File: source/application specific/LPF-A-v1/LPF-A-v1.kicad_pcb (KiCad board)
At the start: 6 copper layers, 32 x 20 mm, 33 parts, among them J1 Conn_01x01_Pin, J2 Conn_01x01_Pin, J3 Conn_01x01_Pin, J4 Conn_01x01_Pin, J5 Conn_01x01_Pin, J6 Conn_01x01_Pin, J7 Conn_01x01_Pin, U1 OPA140, U2 OPA140

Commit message: Added pad for external resistor input
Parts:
- added J8: Conn_01x01_Pin, Manhattan:Manhattan-2mm, F.Cu at (164.5, 101.5)
- R1: footprint Resistor_SMD:R_1206_3216Metric_Pad1.30x1.75mm_HandSolder -> Resistor_SMD:R_0805_2012Metric_Pad1.20x1.40mm_HandSolder
- moved R1 0.75 mm to (140.0, 101.5)
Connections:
- net Debug renamed InR
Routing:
- net InR: track 23.1 -> 26.7 mm
- net In: track 2.20 -> 3.50 mm
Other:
- board text added: "IN R"
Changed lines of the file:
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@@
 	(net 11 "In")
 	(net 12 "Bias")
-	(net 13 "Debug")
+	(net 13 "InR")
 	(net 14 "Net-(U2--)")
 	(net 15 "U2 V+")
@@
 	(net 23 "Net-(U1-+)")
 	(net 24 "Net-(U2-+)")
+	(footprint "Manhattan:Manhattan-2mm"
+		(layer "F.Cu")
+		(at 164.5 101.5)
+		(property "Reference" "J8"
+			(at 0 -1.905 0)
+			(unlocked yes)
+			(layer "F.SilkS")
+			(hide yes)
+			(effects
+				(font
+					(size 1 1)
+					(thickness 0.1)
+				)
+			)
+		)
+		(property "Value" "Conn_01x01_Pin"
+			(at 0 1.675 0)
+			(unlocked yes)
+			(layer "F.Fab")
+			(hide yes)
+			(effects
+				(font
+					(size 1 1)
+					(thickness 0.15)
+				)
+			)
+		)
+		(property "Footprint" "Manhattan:Manhattan-2mm"
+			(at 0 0 0)
+			(unlocked yes)
+			(layer "F.Fab")
+			(hide yes)
+			(effects
+				(font
+					(size 1 1)
+					(thickness 0.15)
+				)
+			)
+		)
+		(property "Datasheet" ""
+			(at 0 0 0)
+			(unlocked yes)
+			(layer "F.Fab")
+			(hide yes)
+			(effects
+				(font
+					(size 1 1)
+					(thickness 0.15)
+				)
+			)
+		)
+		(property "Description" "Generic connector, single row, 01x01, script generated"
+			(at 0 0 0)
+			(unlocked yes)
+			(layer "F.Fab")
+			(hide yes)
+			(effects
+				(font
+					(size 1 1)
+					(thickness 0.15)
+				)
+			)
+		)
+		(property ki_fp_filters "Connector*:*_1x??_*")
+		(sheetname "Root")
+		(sheetfile "LPF-A-v1.kicad_sch")
+		(attr smd)
+		(fp_text user "${REFERENCE}"
+			(at 0 3.175 0)
+			(unlocked yes)
+			(layer "F.Fab")
+			(effects
+				(font
+					(size 1 1)
+					(thickness 0.15)
+				)
+			)
+		)
+		(pad "1" smd roundrect
+			(at 0 0)
+			(size 2 2)
+			(layers "F.Cu" "F.Paste" "F.Mask")
+			(roundrect_rratio 0.125)
+			(net 13 "InR")
+			(pinfunction "Pin_1")
+			(pintype "passive")
+			(thermal_bridge_angle 45)
+		)
+	)
 	(footprint "Resistor_SMD:R_0603_1608Metric_Pad0.98x0.95mm_HandSolder"
 		(layer "F.Cu")
@@
 			(layers "F.Cu" "F.Paste" "F.Mask")
 			(roundrect_rratio 0.15873)
-			(net 13 "Debug")
+			(net 13 "InR")
 			(pintype "passive")
 		)
@@
 			(layers "F.Cu" "F.Paste" "F.Mask")
 			(roundrect_rratio 0.15873)
-			(net 13 "Debug")
+			(net 13 "InR")
 			(pintype "passive")
 		)
@@
 			(layers "F.Cu" "F.Paste" "F.Mask")
 			(roundrect_rratio 0.25)
-			(net 13 "Debug")
+			(net 13 "InR")
 			(pintype "passive")
 		)
@@
 			(layers "F.Cu" "F.Paste" "F.Mask")
 			(roundrect_rratio 0.15873)
-			(net 13 "Debug")
+			(net 13 "InR")
 			(pintype "passive")
 		)
@@
 		)
 	)
-	(footprint "Resistor_SMD:R_1206_3216Metric_Pad1.30x1.75mm_HandSolder"
+	(footprint "Resistor_SMD:R_0805_2012Metric_Pad1.20x1.40mm_HandSolder"
 		(layer "F.Cu")
-		(at 139.25 101.5)
-		(descr "Resistor SMD 1206 (3216 Metric), square (rectangular) end terminal, IPC_7351 nominal with elongated pad for handsoldering. (Body size source: IPC-SM-782 page 72, https://www.pcb-3d.com/wordpress/wp-content/uploads/ipc-sm-782a_amendment_1_and_2.pdf), generated with kicad-footprint-generator")
+		(at 140 101.5)
+		(descr "Resistor SMD 0805 (2012 Metric), square (rectangular) end terminal, IPC_7351 nominal with elongated pad for handsoldering. (Body size source: IPC-SM-782 page 72, https://www.pcb-3d.com/wordpress/wp-content/uploads/ipc-sm-782a_amendment_1_and_2.pdf), generated with kicad-footprint-generator")
 		(tags "resistor handsolder")
 		(property "Reference" "R1"
-			(at 0 -1.82 0)
+			(at 0 -1.65 0)
 			(layer "F.SilkS")
 			(hide yes)
@@
 		)
 		(property "Value" "47k"
-			(at 0 1.82 0)
+			(at 0 1.65 0)
 			(layer "F.Fab")
 			(hide yes)
@@
 			)
 		)
-		(property "Footprint" "Resistor_SMD:R_1206_3216Metric_Pad1.30x1.75mm_HandSolder"
+		(property "Footprint" "Resistor_SMD:R_0805_2012Metric_Pad1.20x1.40mm_HandSolder"
 			(at 0 0 0)
 			(layer "F.Fab")
@@
 		(attr smd)
 		(fp_line
-			(start -0.727064 -0.91)
-			(end 0.727064 -0.91)
+			(start -0.227064 -0.735)
+			(end 0.227064 -0.735)
 			(stroke
 				(width 0.12)
@@
 		)
 		(fp_line
-			(start -0.727064 0.91)
-			(end 0.727064 0.91)
+			(start -0.227064 0.735)
+			(end 0.227064 0.735)
 			(stroke
 				(width 0.12)
@@
 		)
 		(fp_line
-			(start -2.45 -1.12)
-			(end 2.45 -1.12)
+			(start -1.85 -0.95)
+			(end 1.85 -0.95)
 			(stroke
 				(width 0.05)
@@
 		)
 		(fp_line
-			(start -2.45 1.12)
-			(end -2.45 -1.12)
+			(start -1.85 0.95)
+			(end -1.85 -0.95)
 			(stroke
 				(width 0.05)
@@
 		)
 		(fp_line
-			(start 2.45 -1.12)
-			(end 2.45 1.12)
+			(start 1.85 -0.95)
+			(end 1.85 0.95)
 			(stroke
 				(width 0.05)
@@
 		)
 		(fp_line
-			(start 2.45 1.12)
-			(end -2.45 1.12)
+			(start 1.85 0.95)
+			(end -1.85 0.95)
 			(stroke
 				(width 0.05)
@@
 		)
 		(fp_line
-			(start -1.6 -0.8)
-			(end 1.6 -0.8)
+			(start -1 -0.625)
+			(end 1 -0.625)
 			(stroke
 				(width 0.1)
@@
 		)
 		(fp_line
-			(start -1.6 0.8)
-			(end -1.6 -0.8)
+			(start -1 0.625)
+			(end -1 -0.625)
 			(stroke
 				(width 0.1)
@@
 		)
 		(fp_line
-			(start 1.6 -0.8)
-			(end 1.6 0.8)
+			(start 1 -0.625)
+			(end 1 0.625)
 			(stroke
 				(width 0.1)
@@
 		)
 		(fp_line
-			(start 1.6 0.8)
-			(end -1.6 0.8)
+			(start 1 0.625)
+			(end -1 0.625)
 			(stroke
 				(width 0.1)
@@
 			(effects
 				(font
-					(size 0.8 0.8)
-					(thickness 0.12)
+					(size 0.5 0.5)
+					(thickness 0.08)
 				)
 			)
 		)
 		(pad "1" smd roundrect
-			(at -1.55 0)
-			(size 1.3 1.75)
+			(at -1 0)
+			(size 1.2 1.4)
 			(layers "F.Cu" "F.Paste" "F.Mask")
-			(roundrect_rratio 0.192308)
+			(roundrect_rratio 0.208333)
 			(net 11 "In")
 			(pintype "passive")
 		)
 		(pad "2" smd roundrect
-			(at 1.55 0)
-			(size 1.3 1.75)
+			(at 1 0)
+			(size 1.2 1.4)
 			(layers "F.Cu" "F.Paste" "F.Mask")
-			(roundrect_rratio 0.192308)
-			(net 13 "Debug")
+			(roundrect_rratio 0.208333)
+			(net 13 "InR")
 			(pintype "passive")
 		)
-		(model "${KICAD6_3DMODEL_DIR}/Resistor_SMD.3dshapes/R_1206_3216Metric.wrl"
+		(model "${KICAD6_3DMODEL_DIR}/Resistor_SMD.3dshapes/R_0805_2012Metric.wrl"
 			(offset
 				(xyz 0 0 0)
@@
 			(layers "F.Cu" "F.Paste" "F.Mask")
 			(roundrect_rratio 0.15873)
-			(net 13 "Debug")
+			(net 13 "InR")
 			(pintype "passive")
 		)
@@
 	)
 	(gr_text "IN"
-		(at 139.5 103.5 0)
+		(at 136.75 101.5 0)
 		(layer "F.SilkS")
 		(effects
@@
 		)
 	)
+	(gr_text "IN R"
+		(at 163.25 101.5 0)
+		(layer "F.SilkS")
+		(effects
+			(font
+				(size 0.8 0.8)
+				(thickness 0.15)
+				(bold yes)
+			)
+			(justify right)
+		)
+	)
 	(gr_text "BIN"
 		(at 135.5 105.25 0)
@@
 	)
 	(segment
-		(start 137.7 101.5)
+		(start 139 101.5)
 		(end 135.5 101.5)
 		(width 0.6)
@@
 	)
 	(segment
+		(start 162.3625 101.3625)
+		(end 162 101.3625)
+		(width 0.6)
+		(layer "F.Cu")
+		(net 13)
+	)
+	(segment
 		(start 141 101.5)
 		(end 143.8625 101.5)
@@
 	)
 	(segment
+		(start 164.365 101.365)
+		(end 164.5 101.5)
+		(width 0.6)
+		(layer "F.Cu")
+		(net 13)
+	)
+	(segment
+		(start 162.0025 101.365)
+		(end 164.365 101.365)
+		(width 0.6)
+		(layer "F.Cu")
+		(net 13)
+	)
+	(segment
 		(start 143.8625 101.5)
 		(end 144 101.3625)
@@
 	)
 	(segment
-		(start 162.365 103.115)
-		(end 160.6125 101.3625)
+		(start 156 101.3625)
+		(end 144 101.3625)
 		(width 0.6)
 		(layer "F.Cu")
@@
 	)
 	(segment
-		(start 160.6125 101.3625)
-		(end 156 101.3625)
+		(start 162.365 104.0875)
+		(end 162.365 101.365)
 		(width 0.6)
 		(layer "F.Cu")
@@
 	)
 	(segment
-		(start 162.365 104.0875)
-		(end 162.365 103.115)
+		(start 162 101.3625)
+		(end 162.0025 101.365)
 		(width 0.6)
 		(layer "F.Cu")
@@
 	)
 	(segment
-		(start 156 101.3625)
-		(end 144 101.3625)
+		(start 162.365 101.365)
+		(end 162.3625 101.3625)
+		(width 0.6)
+		(layer "F.Cu")
+		(net 13)
+	)
+	(segment
+		(start 162 101.3625)
+		(end 156 101.3625)
 		(width 0.6)
 		(layer "F.Cu")

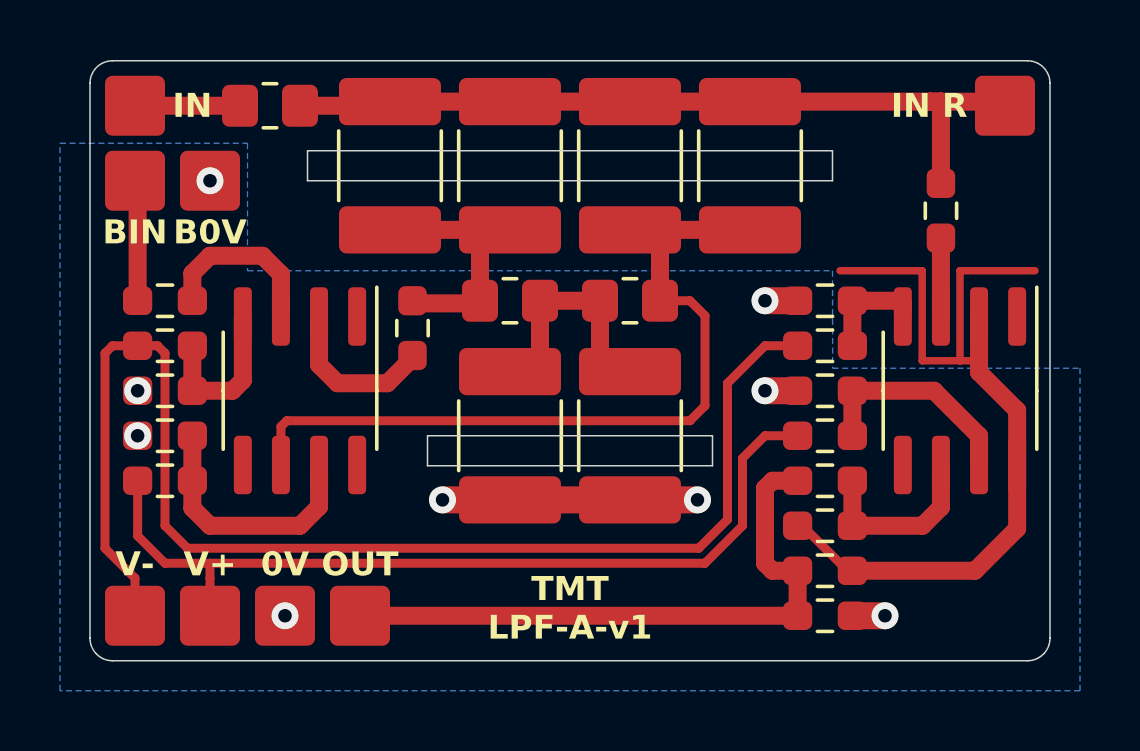
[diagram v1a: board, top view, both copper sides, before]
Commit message: Updated output capacitors to 0805
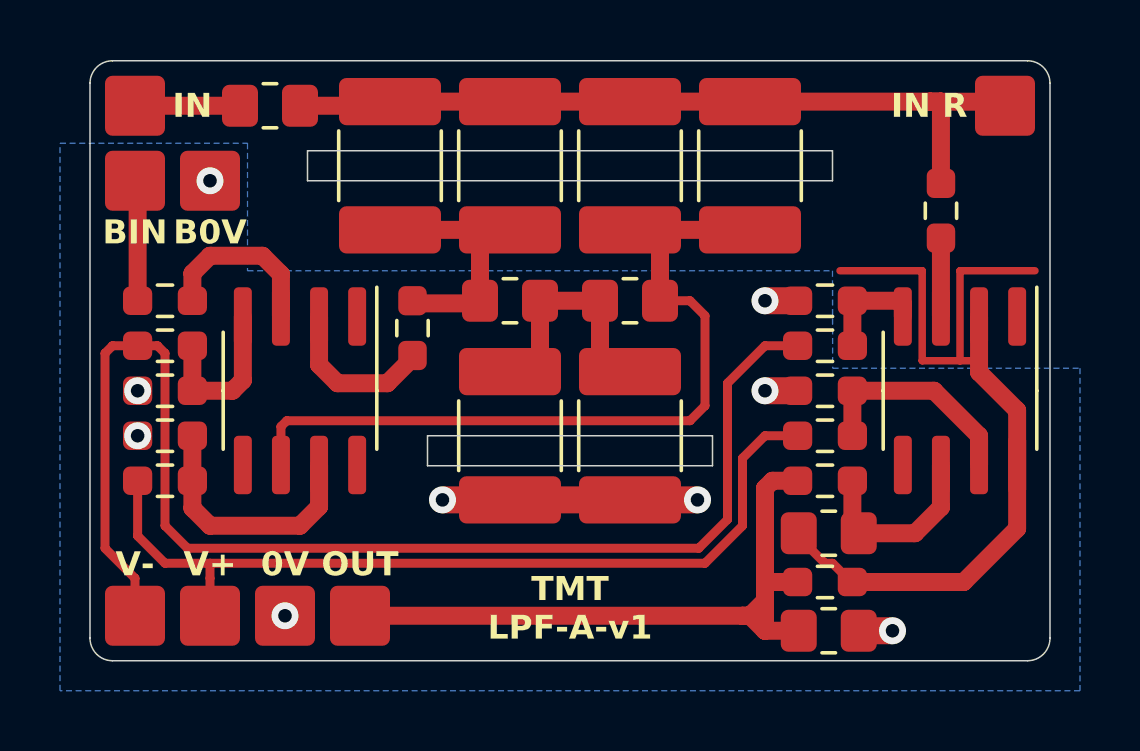
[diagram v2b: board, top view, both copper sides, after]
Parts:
- C7, C8: footprint Resistor_SMD:R_0603_1608Metric_Pad0.98x0.95mm_HandSolder -> Resistor_SMD:R_0805_2012Metric_Pad1.20x1.40mm_HandSolder
- moved C8 0.52 mm to (158.6, 119.0)
- moved R7 0.38 mm to (158.5, 117.4)
- moved C7 0.28 mm to (158.6, 115.8)
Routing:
- net Out: track 21.0 -> 23.6 mm

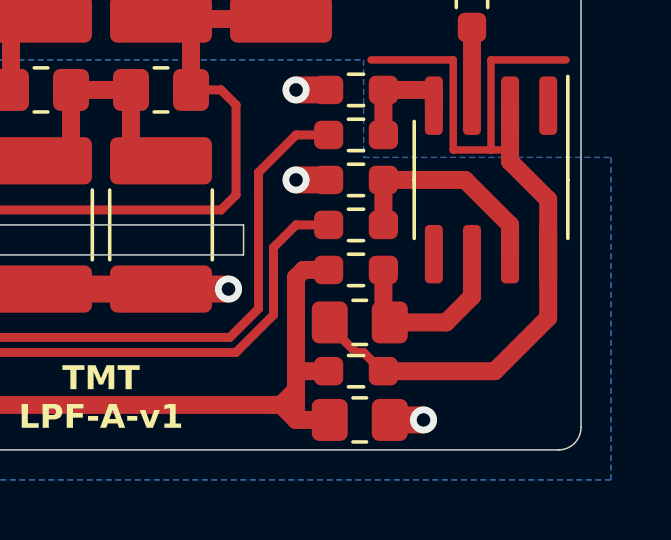
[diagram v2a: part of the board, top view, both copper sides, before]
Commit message: Added pad to allow for external sense
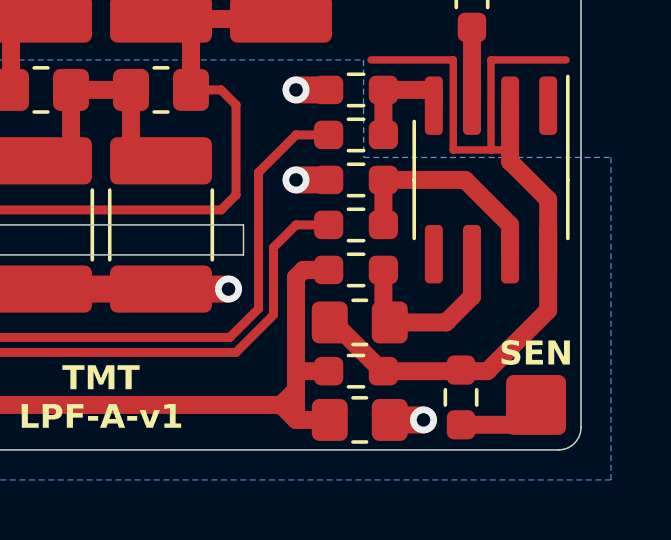
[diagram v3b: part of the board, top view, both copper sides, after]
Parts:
- added J9: Conn_01x01_Pin, Manhattan:Manhattan-2mm, F.Cu at (164.5, 118.5)
- added R13: 2.2k, Resistor_SMD:R_0603_1608Metric_Pad0.98x0.95mm_HandSolder, F.Cu at (162.0, 118.2)
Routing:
- net OutSense: track 0.00 -> 2.77 mm
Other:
- board text added: "SEN"

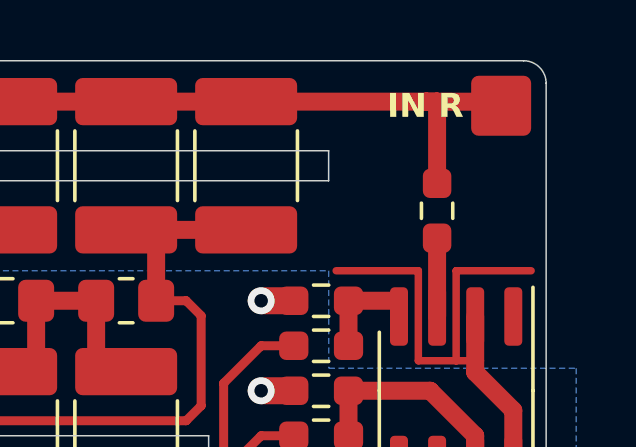
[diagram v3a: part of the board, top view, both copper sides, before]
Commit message: Tweaked silk
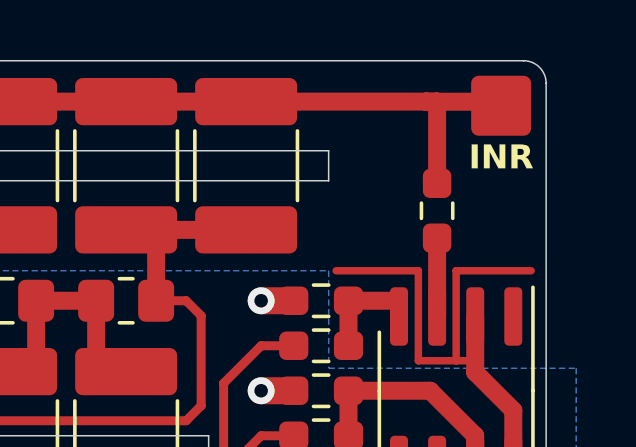
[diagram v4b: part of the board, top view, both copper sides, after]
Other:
- board text added: "INR"
- board text removed: "IN R"
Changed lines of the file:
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@@
 		)
 	)
-	(gr_text "IN R"
-		(at 163.25 101.5 0)
+	(gr_text "INR"
+		(at 164.5 102.75 0)
 		(layer "F.SilkS")
 		(effects
@@
 				(bold yes)
 			)
-			(justify right)
+			(justify top)
 		)
 	)
